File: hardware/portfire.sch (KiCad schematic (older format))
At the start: 30 parts, among them IC101 STM32F4xxVxTx, IC103 25AA02E48, IC104 ADP3335, IC105 SNx5176B, P101 SWD_TC, P102 AUX_BUS_RX, P103 AUX_BUS_RX

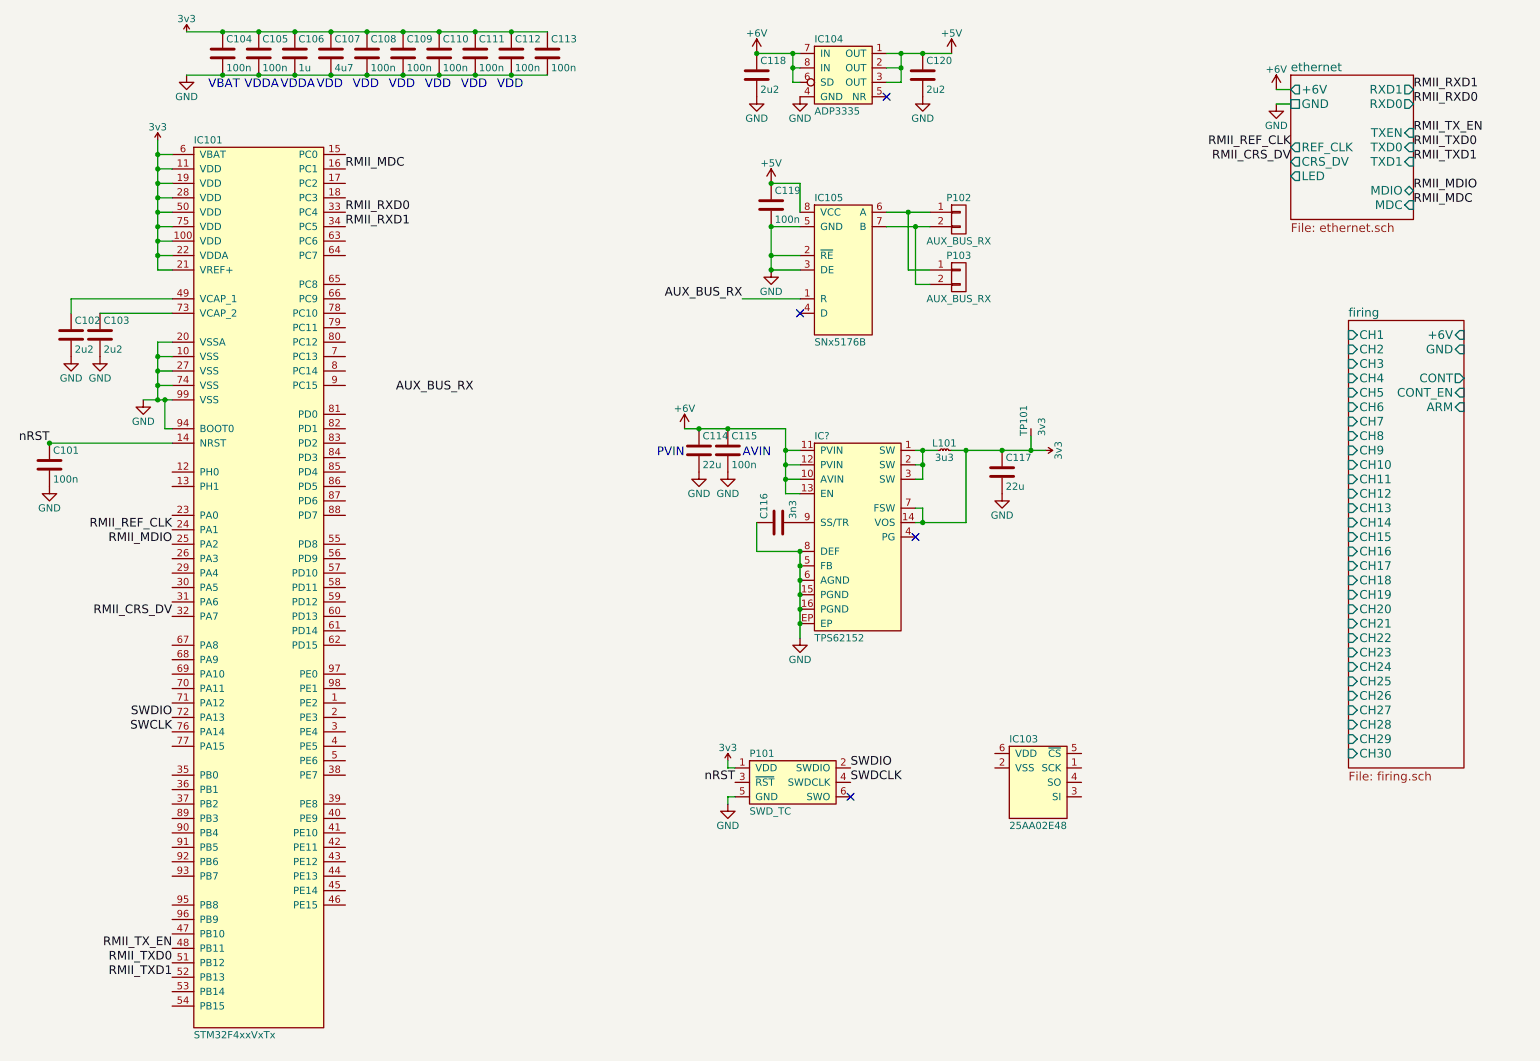
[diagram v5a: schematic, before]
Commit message: LEDs, ethernet jack
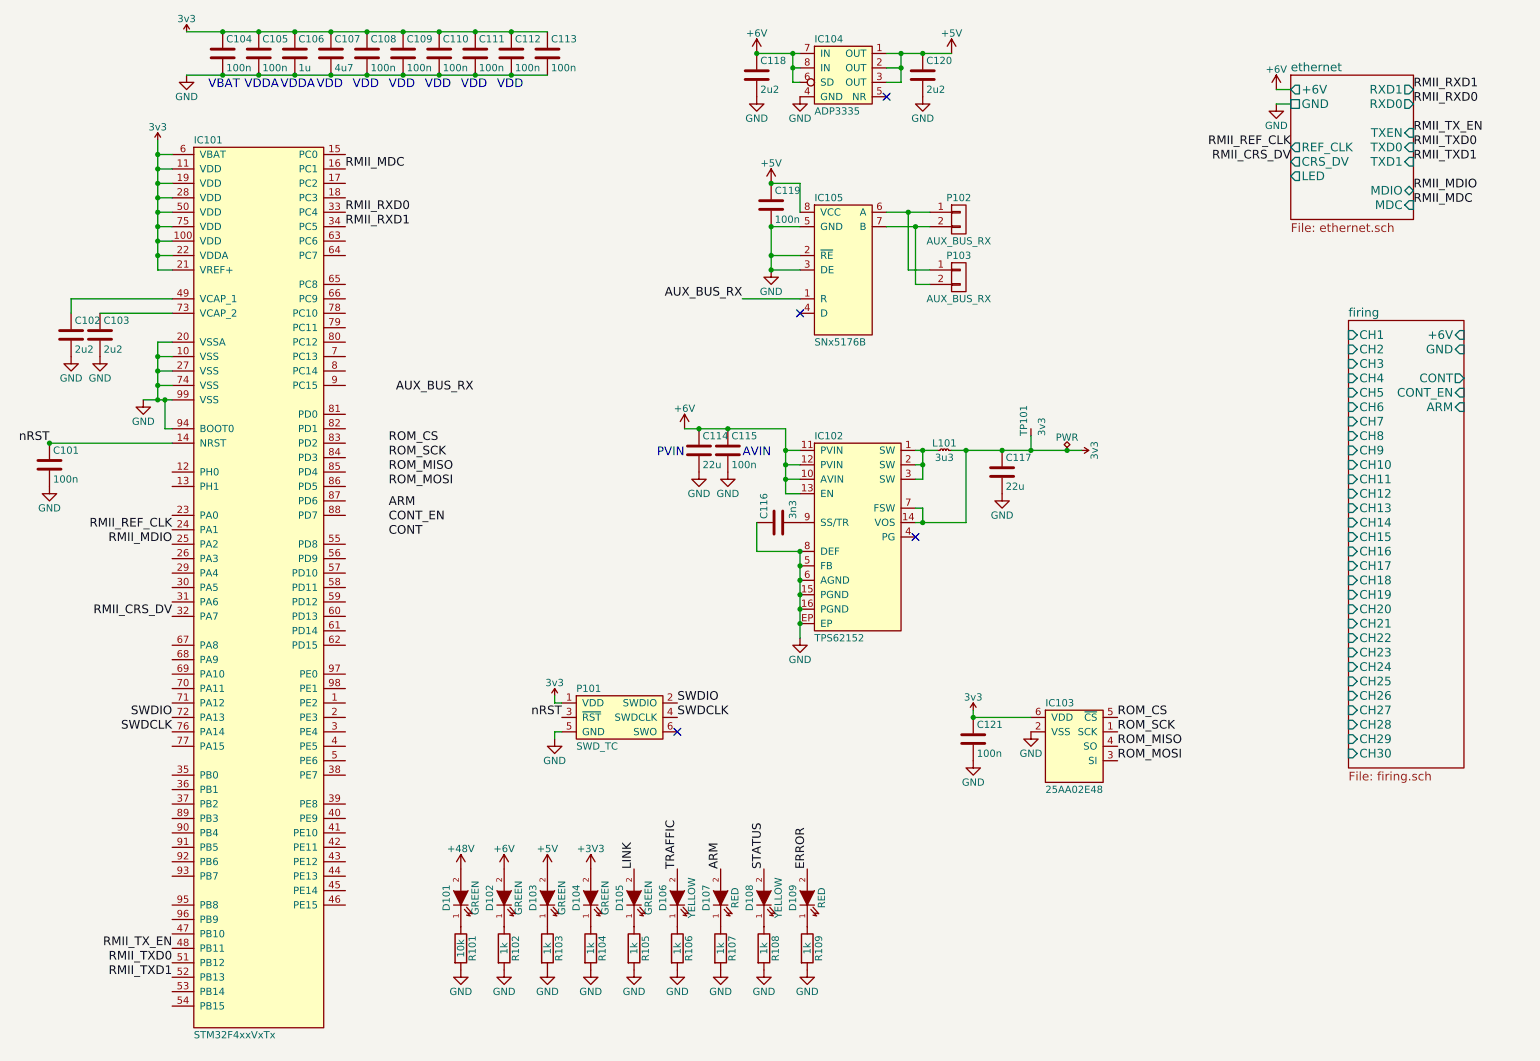
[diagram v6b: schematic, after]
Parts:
- added C121: 100n, agg:0603, symbol C
- added D101, D102, D103, D104, D105: GREEN, agg:0603-LED, symbol LED
- added D106, D108: YELLOW, agg:0603-LED, symbol LED
- added D107, D109: RED, agg:0603-LED, symbol LED
- added R101: 10k, agg:0603, symbol R
- added R102, R103, R104, R105, R106, R107, R108, R109: 1k, agg:0603, symbol R
- gave numbers to parts that had none: 1
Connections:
- net SWCLK is gone; now on net SWDCLK: IC101.76 (PA14)
- net +5V: now also D103.2 (A)
- net +6V: now also D102.2 (A)
- net 3v3: now also IC103.6 (VDD), C121.1
- net GND: now also IC103.2 (VSS), C121.2, R101.2, R102.2, R103.2, R104.2, R105.2, R106.2, R107.2, R108.2, R109.2
- net ROM_SCK: now reaches IC103.1 (SCK)
- net ROM_MOSI: now reaches IC103.3 (SI)
- net ROM_MISO: now reaches IC103.4 (SO)
- net ROM_CS: now reaches IC103.5 (~CS)
- new net: D101.1 (K), R101.1
- new net: D106.1 (K), R106.1
- new net: D107.1 (K), R107.1
- new net: D102.1 (K), R102.1
- new net: D103.1 (K), R103.1
- new net: D104.1 (K), R104.1
- new net: D105.1 (K), R105.1
- new net: D108.1 (K), R108.1
- new net: D109.1 (K), R109.1
- new net +3V3: D104.2 (A)
- new net +48V: D101.2 (A)
- new net ARM: D107.2 (A)
- new net ERROR: D109.2 (A)
- new net LINK: D105.2 (A)
- new net STATUS: D108.2 (A)
- new net TRAFFIC: D106.2 (A)
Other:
- moved on the sheet: IC103, P101

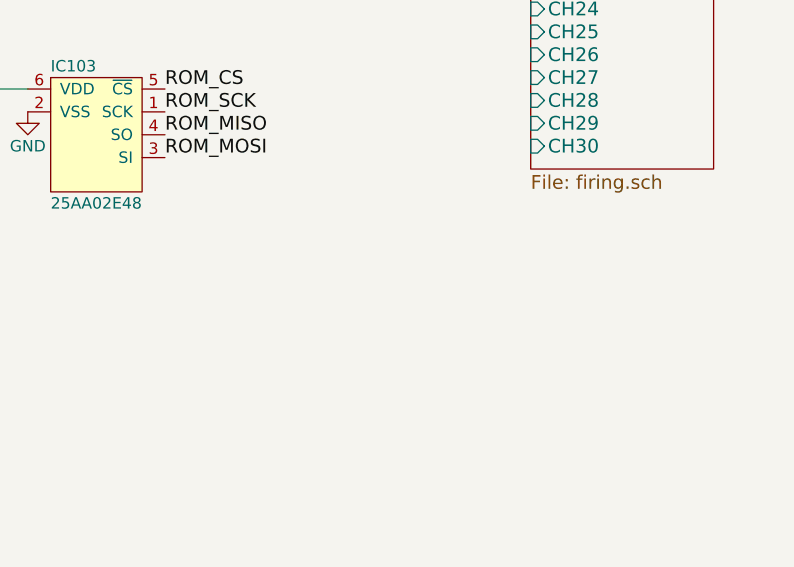
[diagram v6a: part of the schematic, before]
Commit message: mounting holes
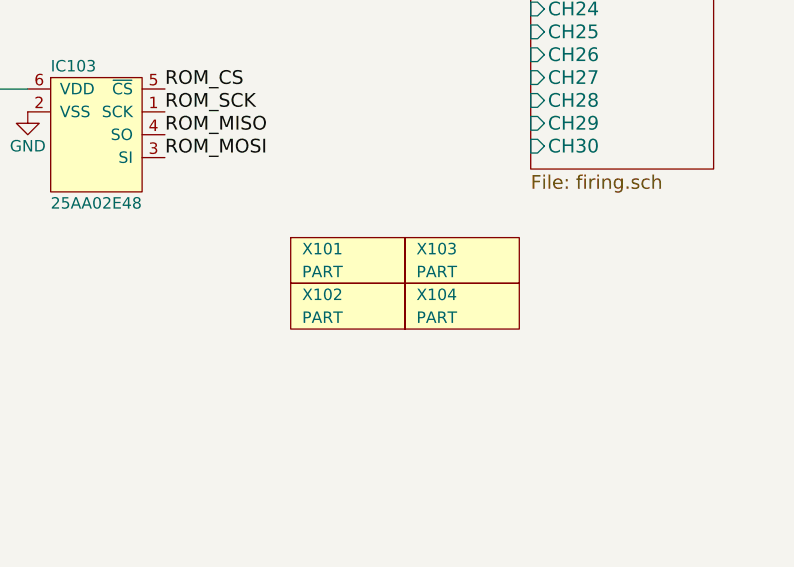
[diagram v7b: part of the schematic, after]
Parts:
- added X101, X102, X103, X104: PART, agg:M3_MOUNT, symbol PART

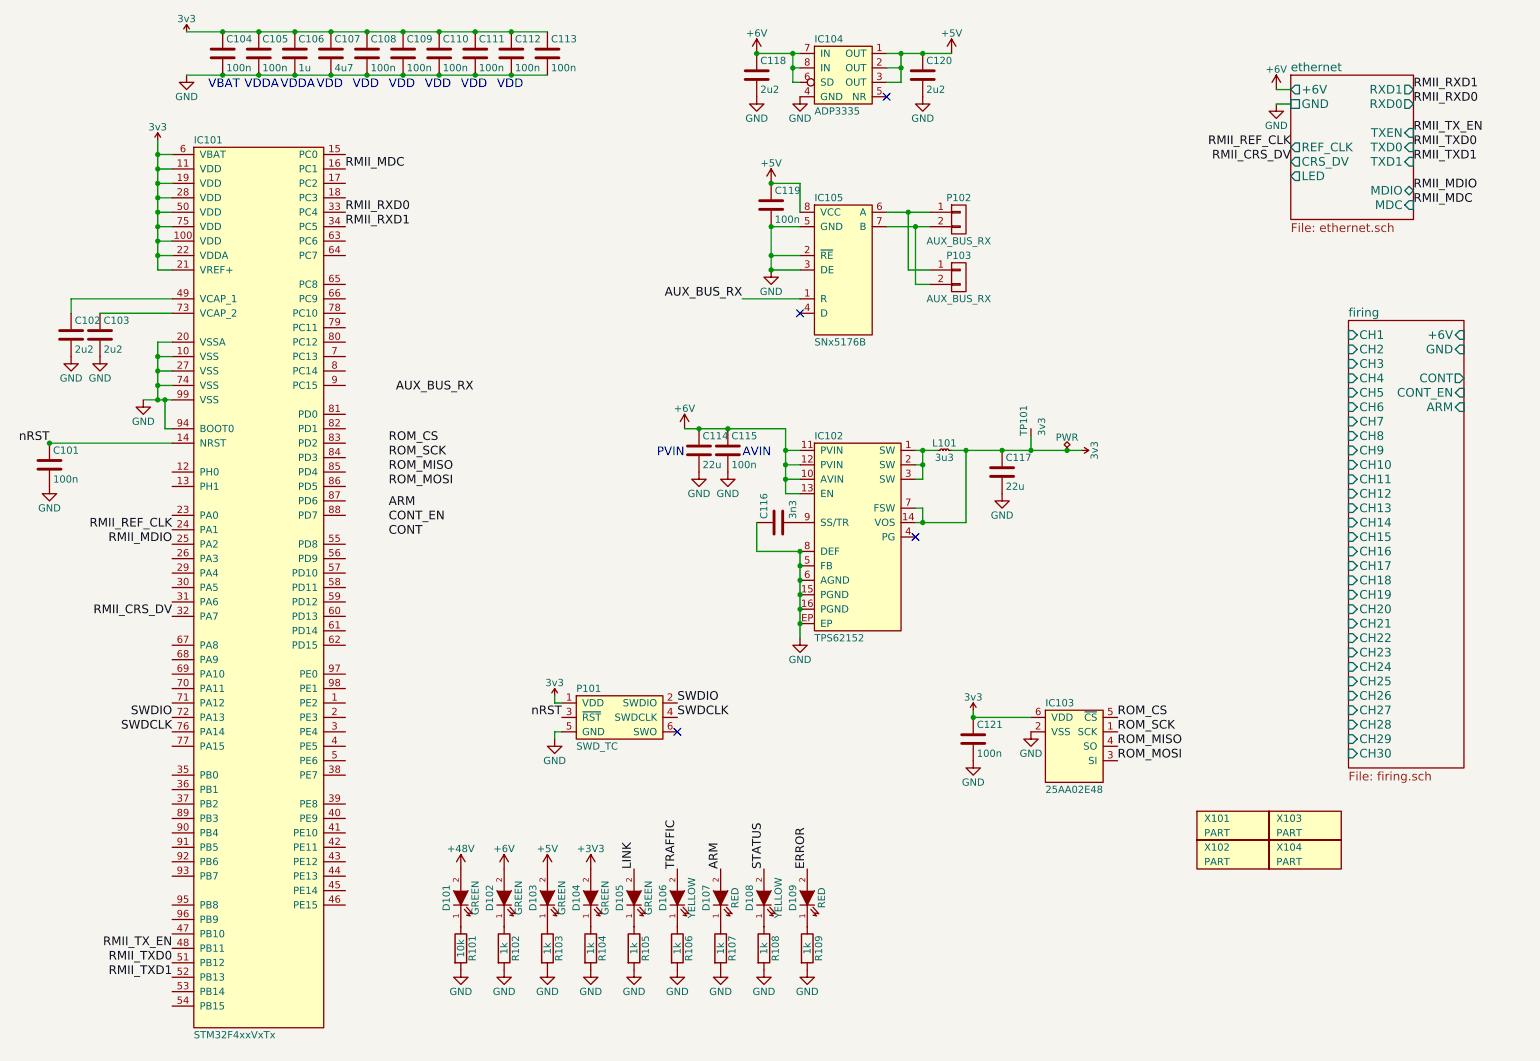
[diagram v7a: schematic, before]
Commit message: Added xtal to STM32
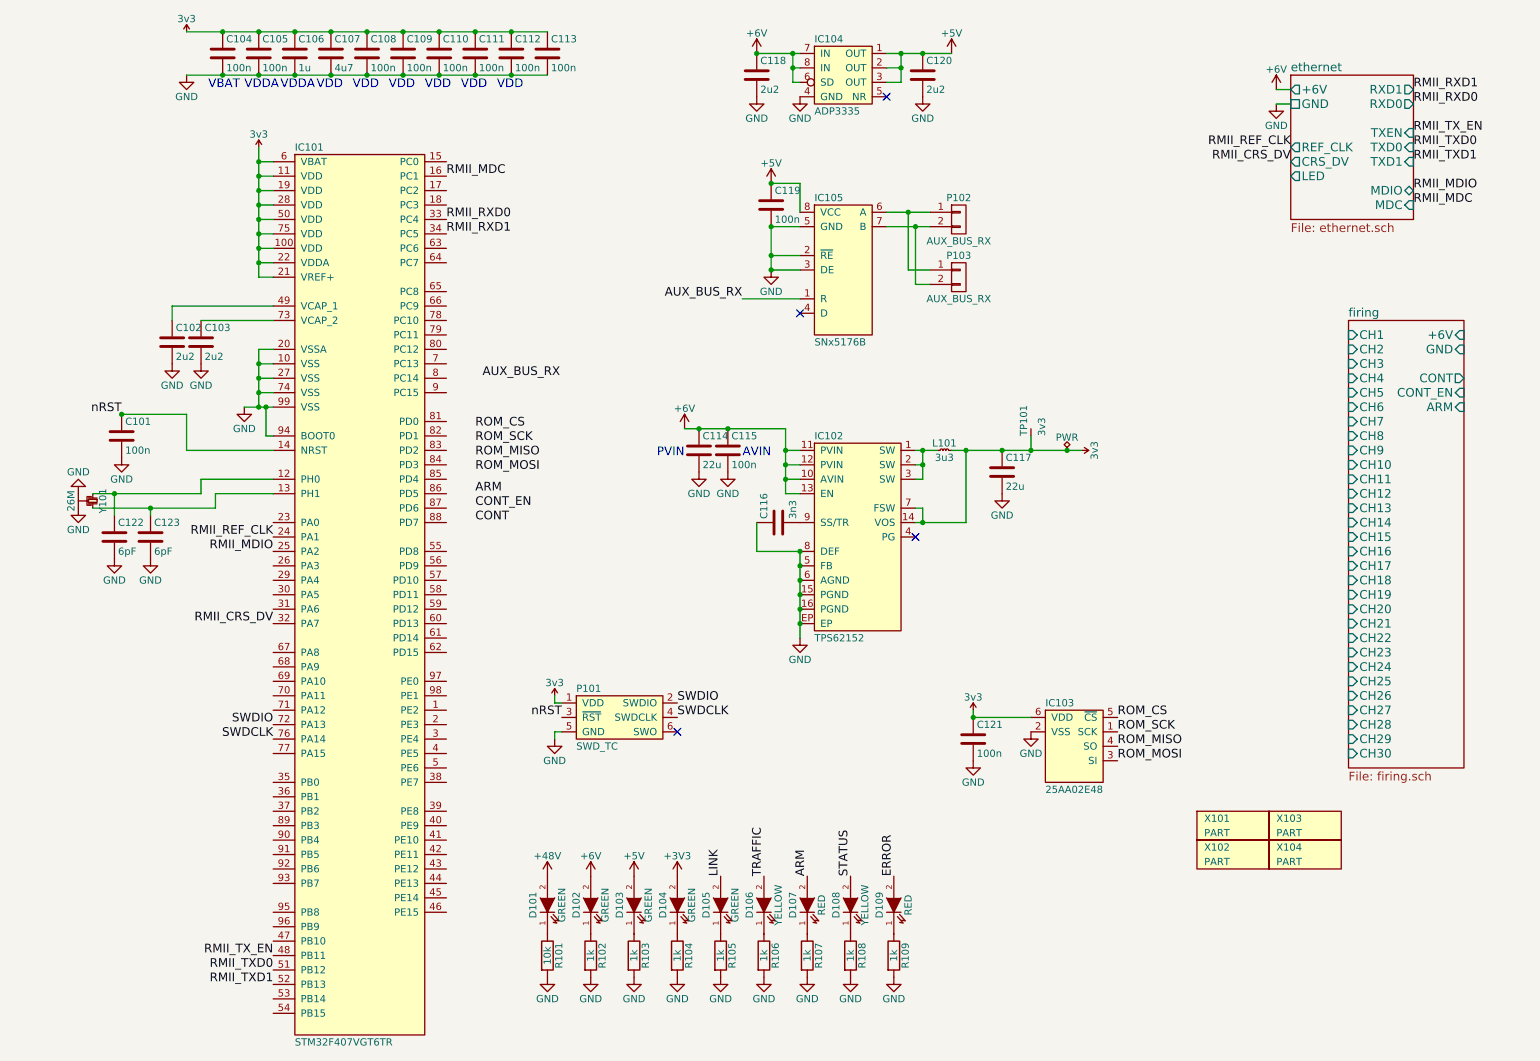
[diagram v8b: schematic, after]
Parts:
- added C122, C123: 6pF, agg:0603, symbol C
- added Y101: 26M, agg:XTAL-20x16, symbol SMD_XTAL
- IC101: value STM32F4xxVxTx -> STM32F407VGT6TR
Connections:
- net GND: now also C122.2, C123.2, Y101.2, Y101.4
- net at IC101.12 (PH0): now also C122.1, Y101.1
- net at IC101.13 (PH1): now also C123.1, Y101.3
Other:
- moved on the sheet: C101, C102, C103, D101, D102, D103, D104, D105, D106, D107, D108, D109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
